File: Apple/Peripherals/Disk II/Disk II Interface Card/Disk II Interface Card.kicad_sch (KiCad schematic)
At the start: 28 parts, among them J1 50 Pin Edge, J2 Drive 2, J3 Drive 1, Q1 2N3906, Q2 MPSU51, Q3 MPSU51

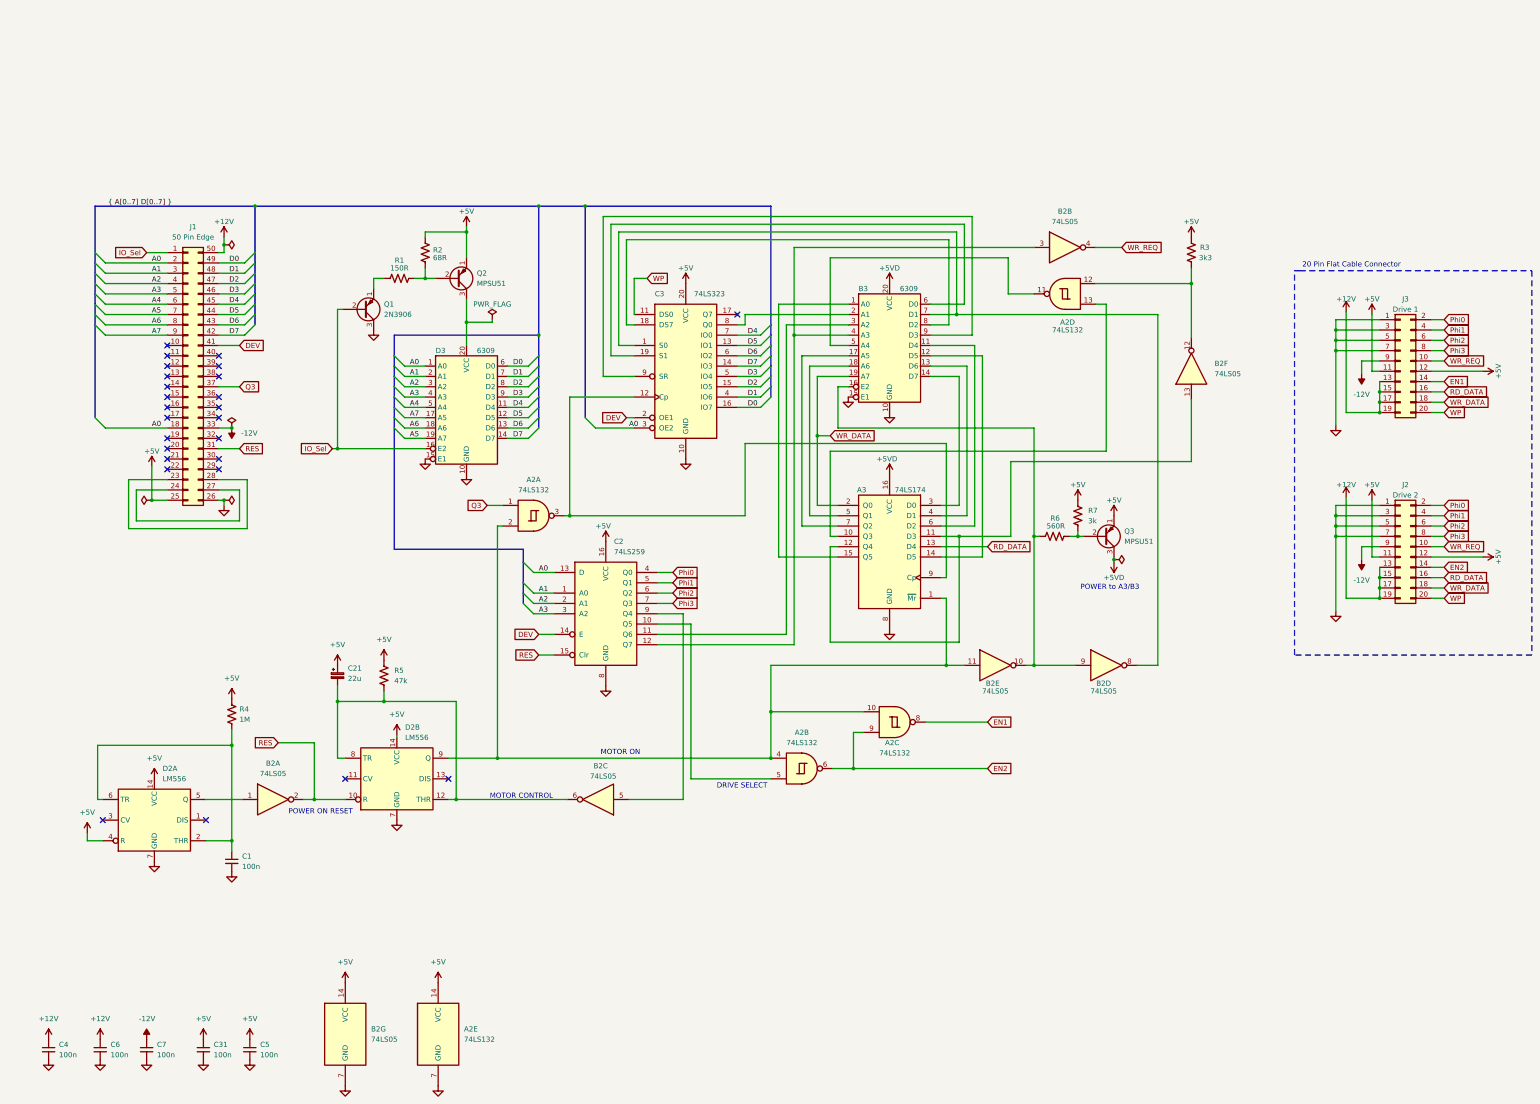
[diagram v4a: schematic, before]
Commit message: changed all ICs to UX#. ERC didn't like the overlap with the capacitor designators. UX# matches the convention in other apple schemaics, even though it wasn't used on the Disk ][.
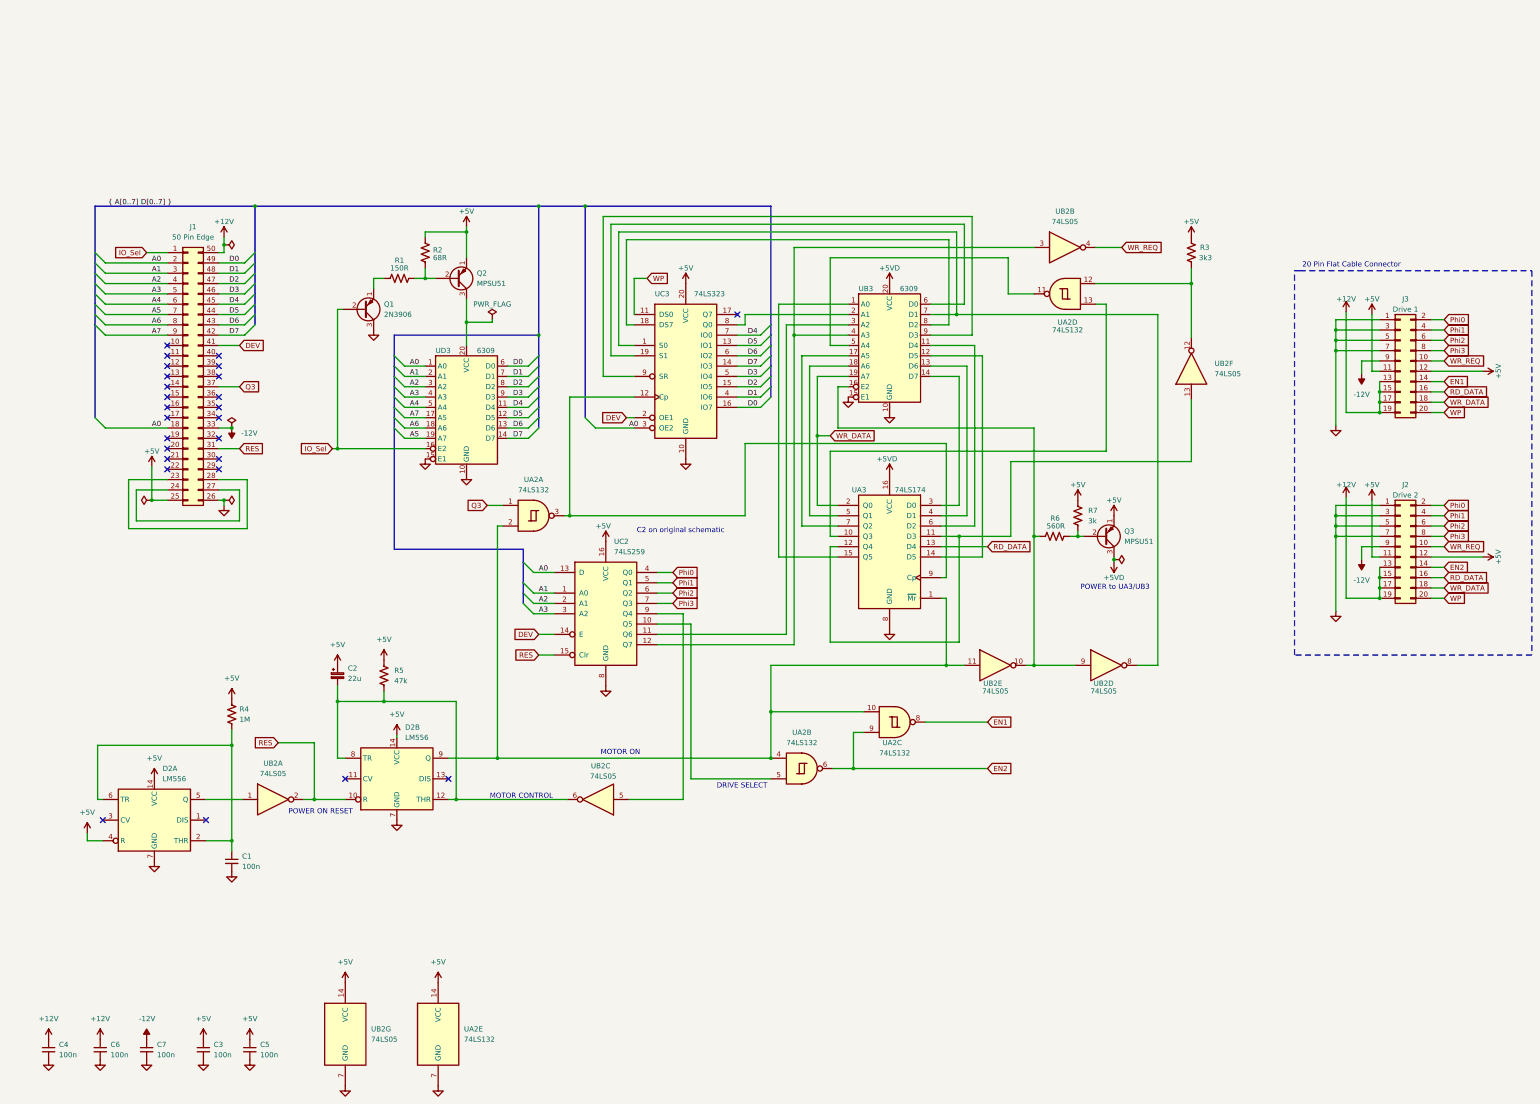
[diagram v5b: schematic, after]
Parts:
- renumbered C21 to C2, C31 to C3, A2 to UA2, A3 to UA3, B2 to UB2, B3 to UB3, C2 to UC2, C3 to UC3, D3 to UD3
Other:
- note added: "C2 on original schematic"
- note added: "POWER to UA3/UB3"
- note removed: "POWER to A3/B3"
- company: (none) -> bald.ee/bitpreserve
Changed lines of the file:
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@@
   (title_block
     (title "650-X104")
+    (date "2023-05-05")
+    (rev "2b")
+    (company "bald.ee/bitpreserve")
     (comment 1 "Apple Disk II Interface Card")
   )
@@
     (effects (font (size 1.27 1.27)) (justify left bottom))
   )
-  (text "POWER to A3/B3" (at 280.035 154.94 0)
+  (text "POWER to UA3/UB3" (at 280.035 154.94 0)
     (effects (font (size 1.27 1.27)) (justify left bottom))
   )
@@
     (effects (font (size 1.27 1.27)) (justify left bottom))
   )
+  (text "C2 on original schematic" (at 170.815 140.97 0)
+    (effects (font (size 1.27 1.27)) (justify left bottom))
+  )
   (text "DRIVE SELECT" (at 190.5 203.835 0)
     (effects (font (size 1.27 1.27)) (justify left bottom))
@@
   (symbol (lib_id "Device:C_Polarized_Small") (at 97.155 175.895 0) (unit 1)
     (in_bom yes) (on_board yes) (dnp no) (fields_autoplaced)
-    (property "Reference" "C21" (at 99.695 174.0788 0)
+    (property "Reference" "C2" (at 99.695 174.0788 0)
       (effects (font (size 1.27 1.27)) (justify left))
     )
@@
       (project "Disk II Interface Card"
         (path "/032f6c56-28f3-4b9c-ab37-057382a8f8c1"
-          (reference "C21") (unit 1)
+          (reference "C2") (unit 1)
         )
       )
@@
   (symbol (lib_id "74xx:74LS05") (at 81.28 206.375 0) (unit 1)
     (in_bom yes) (on_board yes) (dnp no) (fields_autoplaced)
-    (property "Reference" "B2" (at 81.28 197.485 0)
+    (property "Reference" "UB2" (at 81.28 197.485 0)
       (effects (font (size 1.27 1.27)))
     )
@@
       (project "Disk II Interface Card"
         (path "/032f6c56-28f3-4b9c-ab37-057382a8f8c1"
-          (reference "B2") (unit 1)
+          (reference "UB2") (unit 1)
         )
       )
@@
   (symbol (lib_id "74xx:74LS05") (at 259.08 173.355 0) (unit 5)
     (in_bom yes) (on_board yes) (dnp no)
-    (property "Reference" "B2" (at 258.445 177.8 0)
+    (property "Reference" "UB2" (at 258.445 177.8 0)
       (effects (font (size 1.27 1.27)))
     )
@@
       (project "Disk II Interface Card"
         (path "/032f6c56-28f3-4b9c-ab37-057382a8f8c1"
-          (reference "B2") (unit 5)
+          (reference "UB2") (unit 5)
         )
       )
@@
   (symbol (lib_id "74xx:74LS05") (at 99.06 264.16 0) (unit 7)
     (in_bom yes) (on_board yes) (dnp no)
-    (property "Reference" "B2" (at 105.41 262.8899 0)
+    (property "Reference" "UB2" (at 105.41 262.8899 0)
       (effects (font (size 1.27 1.27)) (justify left))
     )
@@
       (project "Disk II Interface Card"
         (path "/032f6c56-28f3-4b9c-ab37-057382a8f8c1"
-          (reference "B2") (unit 7)
+          (reference "UB2") (unit 7)
         )
       )
@@
   (symbol (lib_id "74xx:74LS259") (at 163.195 160.655 0) (unit 1)
     (in_bom yes) (on_board yes) (dnp no) (fields_autoplaced)
-    (property "Reference" "C2" (at 165.2144 142.875 0)
+    (property "Reference" "UC2" (at 165.2144 142.875 0)
       (effects (font (size 1.27 1.27)) (justify left))
     )
@@
       (project "Disk II Interface Card"
         (path "/032f6c56-28f3-4b9c-ab37-057382a8f8c1"
-          (reference "C2") (unit 1)
+          (reference "UC2") (unit 1)
         )
       )
@@
   (symbol (lib_id "74xx:74LS132") (at 276.225 81.915 0) (mirror y) (unit 4)
     (in_bom yes) (on_board yes) (dnp no)
-    (property "Reference" "A2" (at 276.86 88.9 0)
+    (property "Reference" "UA2" (at 276.86 88.9 0)
       (effects (font (size 1.27 1.27)))
     )
@@
       (project "Disk II Interface Card"
         (path "/032f6c56-28f3-4b9c-ab37-057382a8f8c1"
-          (reference "A2") (unit 4)
+          (reference "UA2") (unit 4)
         )
       )
@@
   (symbol (lib_id "74xx:74LS132") (at 121.92 264.16 0) (unit 5)
     (in_bom yes) (on_board yes) (dnp no) (fields_autoplaced)
-    (property "Reference" "A2" (at 128.27 262.8899 0)
+    (property "Reference" "UA2" (at 128.27 262.8899 0)
       (effects (font (size 1.27 1.27)) (justify left))
     )
@@
       (project "Disk II Interface Card"
         (path "/032f6c56-28f3-4b9c-ab37-057382a8f8c1"
-          (reference "A2") (unit 5)
+          (reference "UA2") (unit 5)
         )
       )
@@
   (symbol (lib_id "Device:C_Small") (at 64.135 267.97 0) (unit 1)
     (in_bom yes) (on_board yes) (dnp no) (fields_autoplaced)
-    (property "Reference" "C31" (at 66.675 266.7062 0)
+    (property "Reference" "C3" (at 66.675 266.7062 0)
       (effects (font (size 1.27 1.27)) (justify left))
     )
@@
       (project "Disk II Interface Card"
         (path "/032f6c56-28f3-4b9c-ab37-057382a8f8c1"
-          (reference "C31") (unit 1)
+          (reference "C3") (unit 1)
         )
       )
@@
   (symbol (lib_id "74xx:74LS05") (at 276.225 70.485 0) (unit 2)
     (in_bom yes) (on_board yes) (dnp no) (fields_autoplaced)
-    (property "Reference" "B2" (at 276.225 61.595 0)
+    (property "Reference" "UB2" (at 276.225 61.595 0)
       (effects (font (size 1.27 1.27)))
     )
@@
       (project "Disk II Interface Card"
         (path "/032f6c56-28f3-4b9c-ab37-057382a8f8c1"
-          (reference "B2") (unit 2)
+          (reference "UB2") (unit 2)
         )
       )
@@
   (symbol (lib_id "74xx:74LS05") (at 161.29 206.375 180) (unit 3)
     (in_bom yes) (on_board yes) (dnp no)
-    (property "Reference" "B2" (at 161.925 198.12 0)
+    (property "Reference" "UB2" (at 161.925 198.12 0)
       (effects (font (size 1.27 1.27)))
     )
@@
       (project "Disk II Interface Card"
         (path "/032f6c56-28f3-4b9c-ab37-057382a8f8c1"
-          (reference "B2") (unit 3)
+          (reference "UB2") (unit 3)
         )
       )
@@
   (symbol (lib_id "74xx:74LS132") (at 211.455 198.755 0) (unit 2)
     (in_bom yes) (on_board yes) (dnp no) (fields_autoplaced)
-    (property "Reference" "A2" (at 211.455 189.865 0)
+    (property "Reference" "UA2" (at 211.455 189.865 0)
       (effects (font (size 1.27 1.27)))
     )
@@
       (project "Disk II Interface Card"
         (path "/032f6c56-28f3-4b9c-ab37-057382a8f8c1"
-          (reference "A2") (unit 2)
+          (reference "UA2") (unit 2)
         )
       )
@@
   (symbol (lib_id "74xx:74LS05") (at 307.34 100.33 90) (unit 6)
     (in_bom yes) (on_board yes) (dnp no) (fields_autoplaced)
-    (property "Reference" "B2" (at 313.055 99.0599 90)
+    (property "Reference" "UB2" (at 313.055 99.0599 90)
       (effects (font (size 1.27 1.27)) (justify right))
     )
@@
       (project "Disk II Interface Card"
         (path "/032f6c56-28f3-4b9c-ab37-057382a8f8c1"
-          (reference "B2") (unit 6)
+          (reference "UB2") (unit 6)
         )
       )
@@
   (symbol (lib_id "74xx:74LS132") (at 234.315 187.325 0) (mirror x) (unit 3)
     (in_bom yes) (on_board yes) (dnp no)
-    (property "Reference" "A2" (at 233.68 192.405 0)
+    (property "Reference" "UA2" (at 233.68 192.405 0)
       (effects (font (size 1.27 1.27)))
     )
@@
       (project "Disk II Interface Card"
         (path "/032f6c56-28f3-4b9c-ab37-057382a8f8c1"
-          (reference "A2") (unit 3)
+          (reference "UA2") (unit 3)
         )
       )
@@
   (symbol (lib_id "74xx:74LS174") (at 233.045 144.145 0) (mirror y) (unit 1)
     (in_bom yes) (on_board yes) (dnp no)
-    (property "Reference" "A3" (at 227.33 130.175 0)
+    (property "Reference" "UA3" (at 227.33 130.175 0)
       (effects (font (size 1.27 1.27)) (justify left))
     )
@@
       (project "Disk II Interface Card"
         (path "/032f6c56-28f3-4b9c-ab37-057382a8f8c1"
-          (reference "A3") (unit 1)
+          (reference "UA3") (unit 1)
         )
       )
@@
   (symbol (lib_id "Disk Interface Card:6309") (at 128.905 104.775 0) (unit 1)
     (in_bom yes) (on_board yes) (dnp no)
-    (property "Reference" "D3" (at 121.285 95.885 0)
+    (property "Reference" "UD3" (at 121.285 95.885 0)
       (effects (font (size 1.27 1.27)) (justify left))
     )
@@
       (project "Disk II Interface Card"
         (path "/032f6c56-28f3-4b9c-ab37-057382a8f8c1"
-          (reference "D3") (unit 1)
+          (reference "UD3") (unit 1)
         )
       )
@@
   (symbol (lib_id "74xx:74LS323") (at 182.88 99.695 0) (unit 1)
     (in_bom yes) (on_board yes) (dnp no)
-    (property "Reference" "C3" (at 175.26 81.915 0)
+    (property "Reference" "UC3" (at 175.26 81.915 0)
       (effects (font (size 1.27 1.27)) (justify left))
     )
@@
       (project "Disk II Interface Card"
         (path "/032f6c56-28f3-4b9c-ab37-057382a8f8c1"
-          (reference "C3") (unit 1)
+          (reference "UC3") (unit 1)
         )
       )
@@
   (symbol (lib_id "74xx:74LS05") (at 286.385 173.355 0) (unit 4)
     (in_bom yes) (on_board yes) (dnp no)
-    (property "Reference" "B2" (at 285.75 177.8 0)
+    (property "Reference" "UB2" (at 285.75 177.8 0)
       (effects (font (size 1.27 1.27)))
     )
@@
       (project "Disk II Interface Card"
         (path "/032f6c56-28f3-4b9c-ab37-057382a8f8c1"
-          (reference "B2") (unit 4)
+          (reference "UB2") (unit 4)
         )
       )
@@
   (symbol (lib_id "74xx:74LS132") (at 145.415 136.525 0) (unit 1)
     (in_bom yes) (on_board yes) (dnp no) (fields_autoplaced)
-    (property "Reference" "A2" (at 145.415 127.635 0)
+    (property "Reference" "UA2" (at 145.415 127.635 0)
       (effects (font (size 1.27 1.27)))
     )
@@
       (project "Disk II Interface Card"
         (path "/032f6c56-28f3-4b9c-ab37-057382a8f8c1"
-          (reference "A2") (unit 1)
+          (reference "UA2") (unit 1)
         )
       )
@@
   (symbol (lib_id "Disk Interface Card:6309") (at 233.045 89.535 0) (unit 1)
     (in_bom yes) (on_board yes) (dnp no)
-    (property "Reference" "B3" (at 225.425 80.645 0)
+    (property "Reference" "UB3" (at 225.425 80.645 0)
       (effects (font (size 1.27 1.27)) (justify left))
     )
@@
       (project "Disk II Interface Card"
         (path "/032f6c56-28f3-4b9c-ab37-057382a8f8c1"
-          (reference "B3") (unit 1)
+          (reference "UB3") (unit 1)
         )
       )
